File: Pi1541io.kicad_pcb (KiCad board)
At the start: 2 copper layers, 65 x 56 mm, 56 parts, among them J1 IEC1, J10 SDA, J11 SCL, J12 I2C, J13 SDA, J14 SDA, J15 SDA, J2 IEC2, J3 IEC3, J4 ExtSpkr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

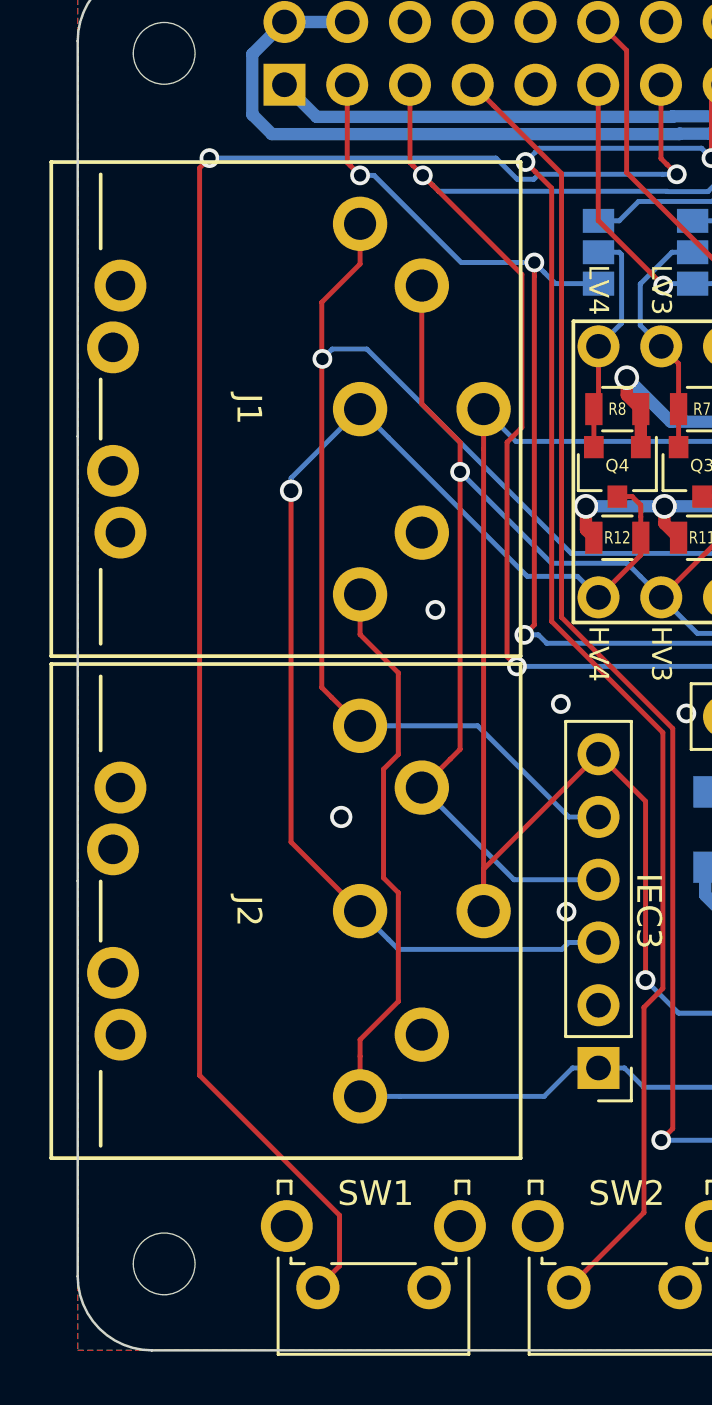
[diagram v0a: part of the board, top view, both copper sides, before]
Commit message: Improved ziptie holes.
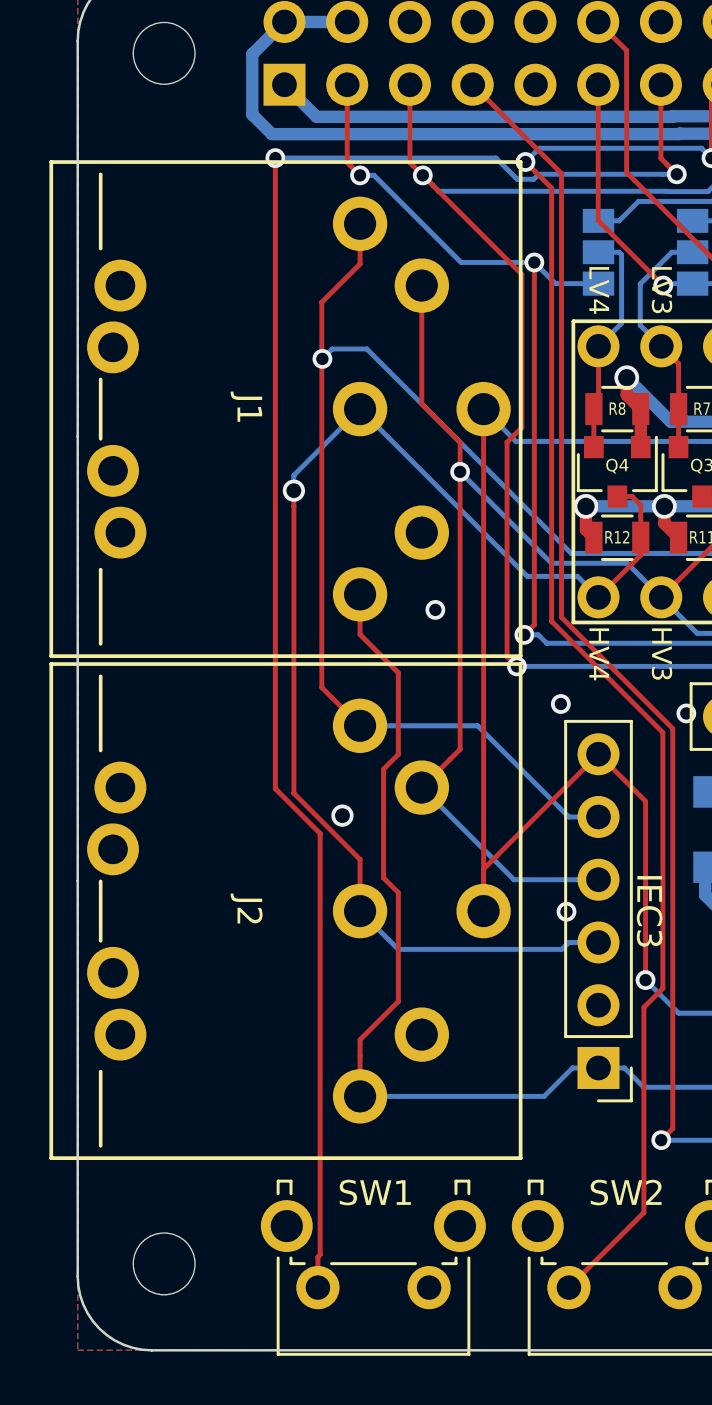
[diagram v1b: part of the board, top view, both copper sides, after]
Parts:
- MK5, MK6: footprint DIN-Connector:ZipTie_2.7mm -> DIN-Connector:ZipTie_3.0mm
- moved MK5 1.12 mm to (111.8, 94.5)
- moved MK6 1.12 mm to (111.8, 100.3)
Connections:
- P1 pad 10: /GPIO15(RXD0) -> (no net)
- P1 pad 19: /GPIO10(SPI0_MOSI) -> (no net)
- P1 pad 21: /GPIO9(SPI0_MISO) -> (no net)
- P1 pad 23: /GPIO11(SPI0_SCK) -> (no net)
- P1 pad 24: /GPIO8(SPI0_CE_N) -> (no net)
- P1 pad 26: /GPIO7(SPI1_CE_N) -> (no net)
- P1 pad 31: /GPIO6 -> (no net)
- P1 pad 32: /GPIO12(PWM0) -> (no net)
- P1 pad 8: /GPIO14(TXD0) -> (no net)
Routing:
- net /GPIO27(GEN2): track 71.8 -> 67.1 mm

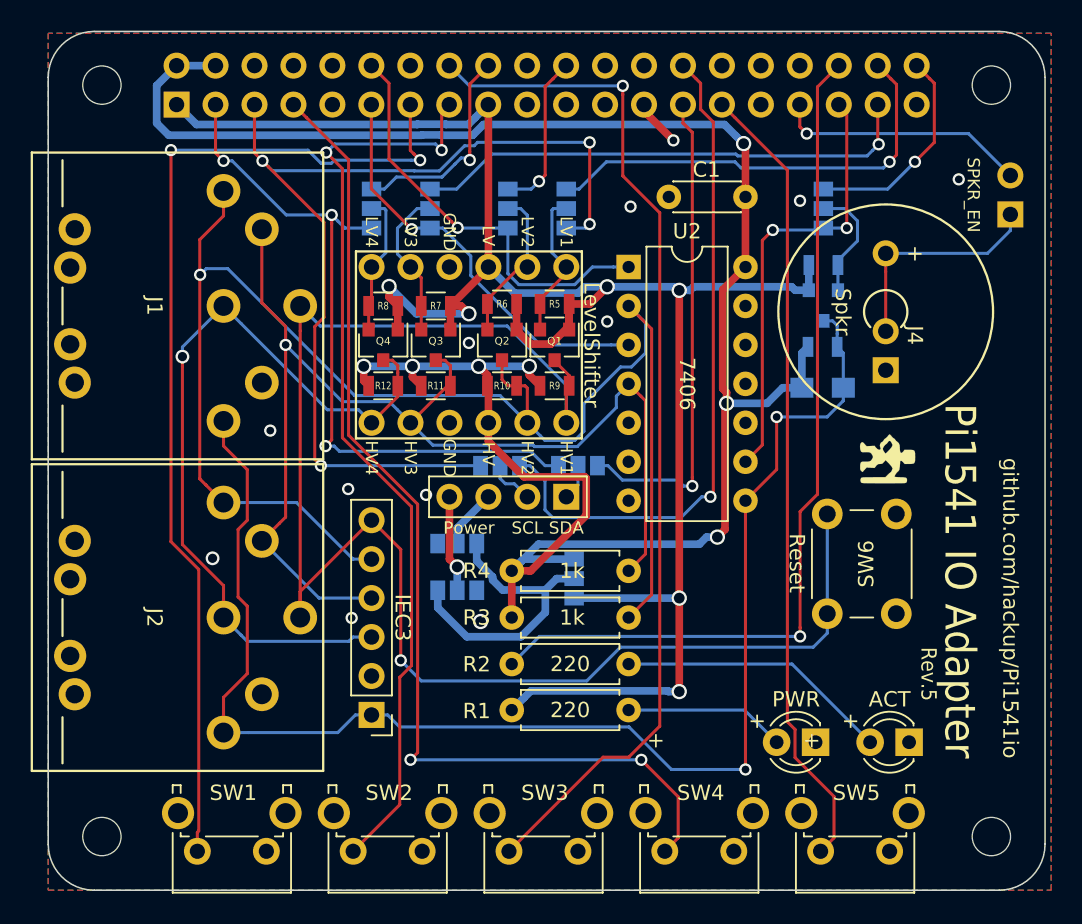
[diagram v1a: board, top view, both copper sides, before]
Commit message: Shuffling layout to move the display connector.
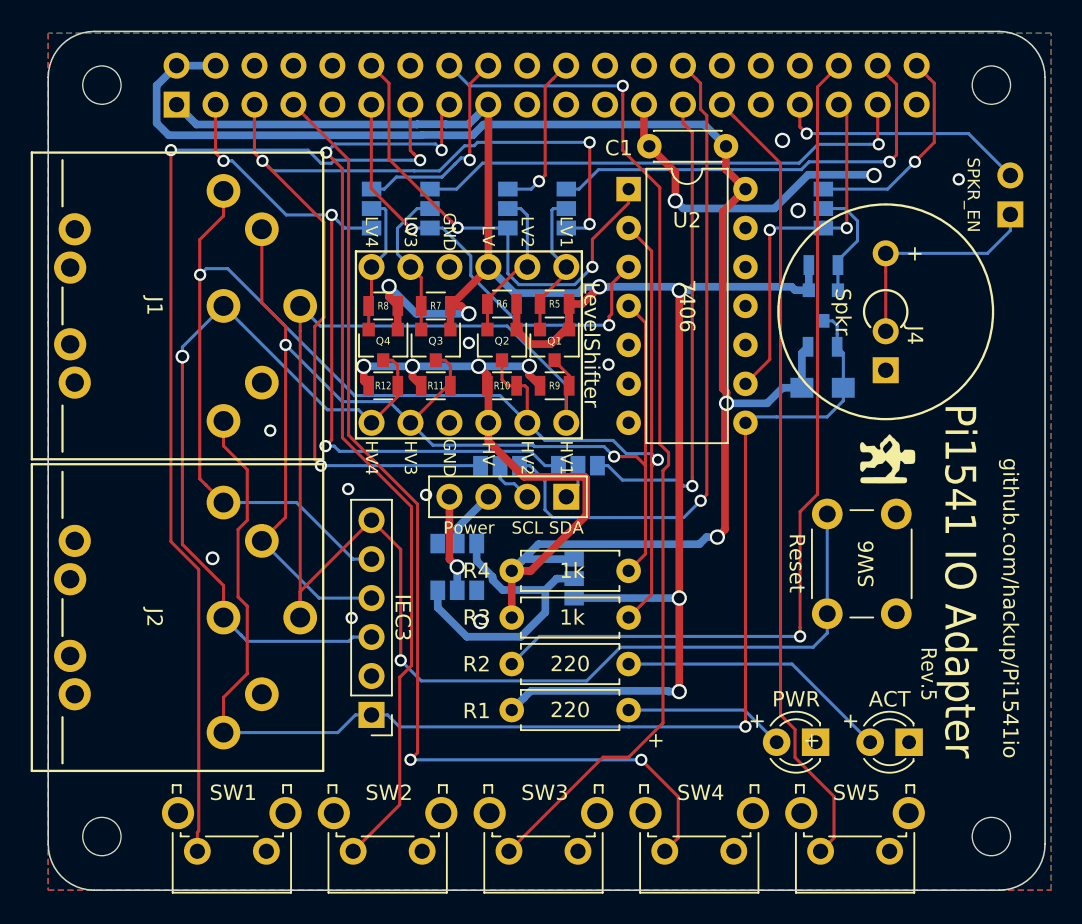
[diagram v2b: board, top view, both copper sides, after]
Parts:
- moved U2 5.08 mm to (144.0, 69.5)
- moved C1 3.54 mm to (150.3, 66.7)
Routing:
- net GND: track 3.13 -> 21.6 mm, vias 12 -> 13
- net SRQ_BD: track 29.0 -> 24.0 mm
- net CLK: track 76.7 -> 81.4 mm, vias 1 -> 2
- net DATA_BD: track 27.8 -> 31.5 mm, vias 1 -> 2
- net SRQ: track 92.8 -> 89.8 mm, vias 2 -> 1
- net CLK_BD: track 27.3 -> 29.8 mm, vias 1 -> 2
- net /GPIO5: track 52.1 -> 53.3 mm
- net +5V: track 139.4 -> 138.6 mm, vias 7 -> 6
- net I2C0_SCL: track 44.7 -> 44.1 mm
- net +3V3: track 127.8 -> 127.2 mm
- net DATA: vias 1 -> 2

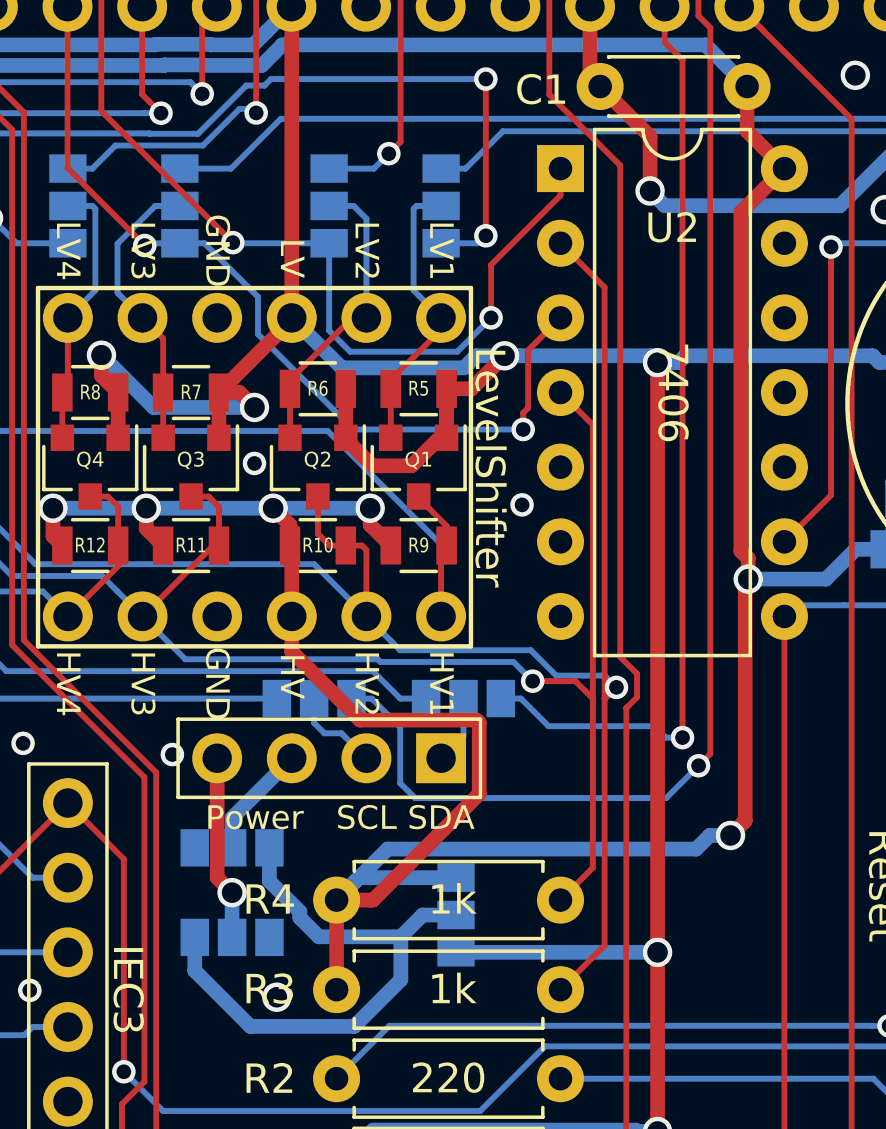
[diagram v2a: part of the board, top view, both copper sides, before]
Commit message: Shuffling layout to move the display connector.
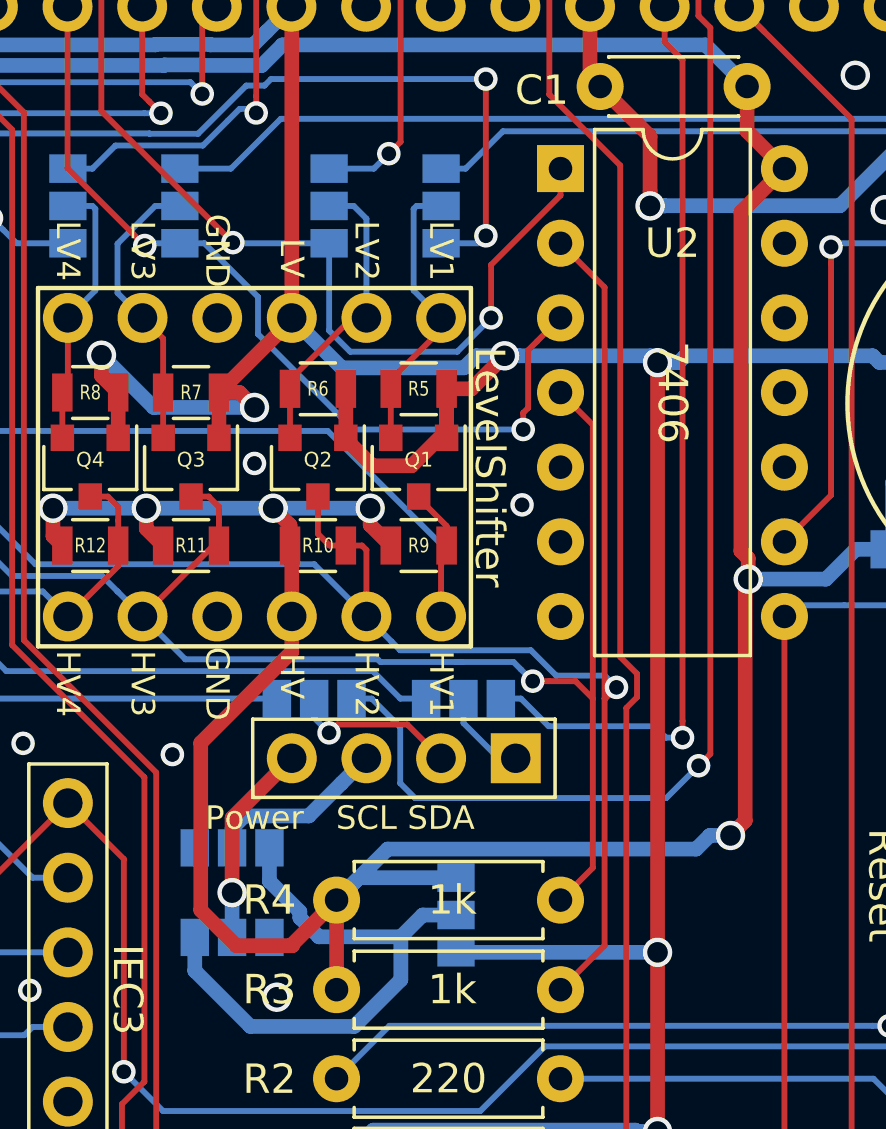
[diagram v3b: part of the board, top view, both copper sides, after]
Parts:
- moved J12 2.54 mm to (142.5, 89.5)
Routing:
- net Net-(J11-Pad2): track 3.11 -> 5.78 mm, vias 0 -> 1
- net Net-(J12-Pad3): track 3.89 -> 6.22 mm
- net Net-(J10-Pad2): track 2.35 -> 3.11 mm
- net Net-(J12-Pad4): track 6.31 -> 6.94 mm
